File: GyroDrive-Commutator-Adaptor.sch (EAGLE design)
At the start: 30 parts, among them IC1 INA2141U, IC2 INA2141U, IC3 INA2141U

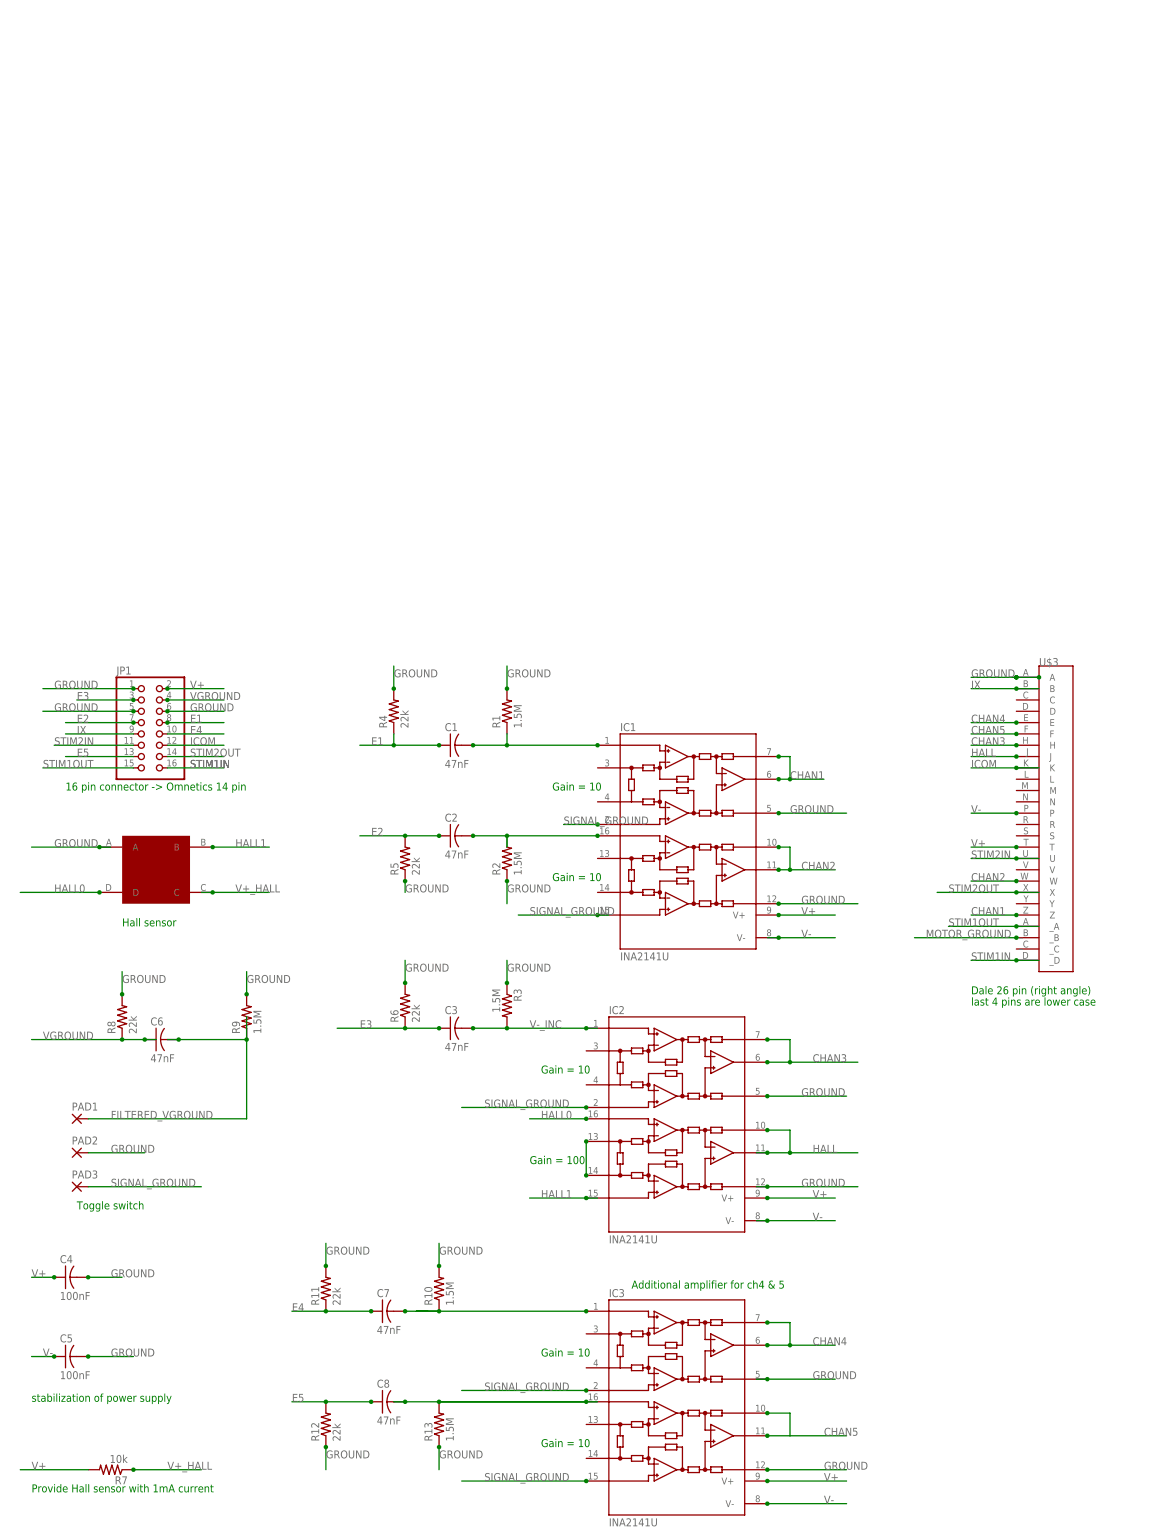
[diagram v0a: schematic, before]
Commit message: Removed VGROUND and changed JMP1 pinout
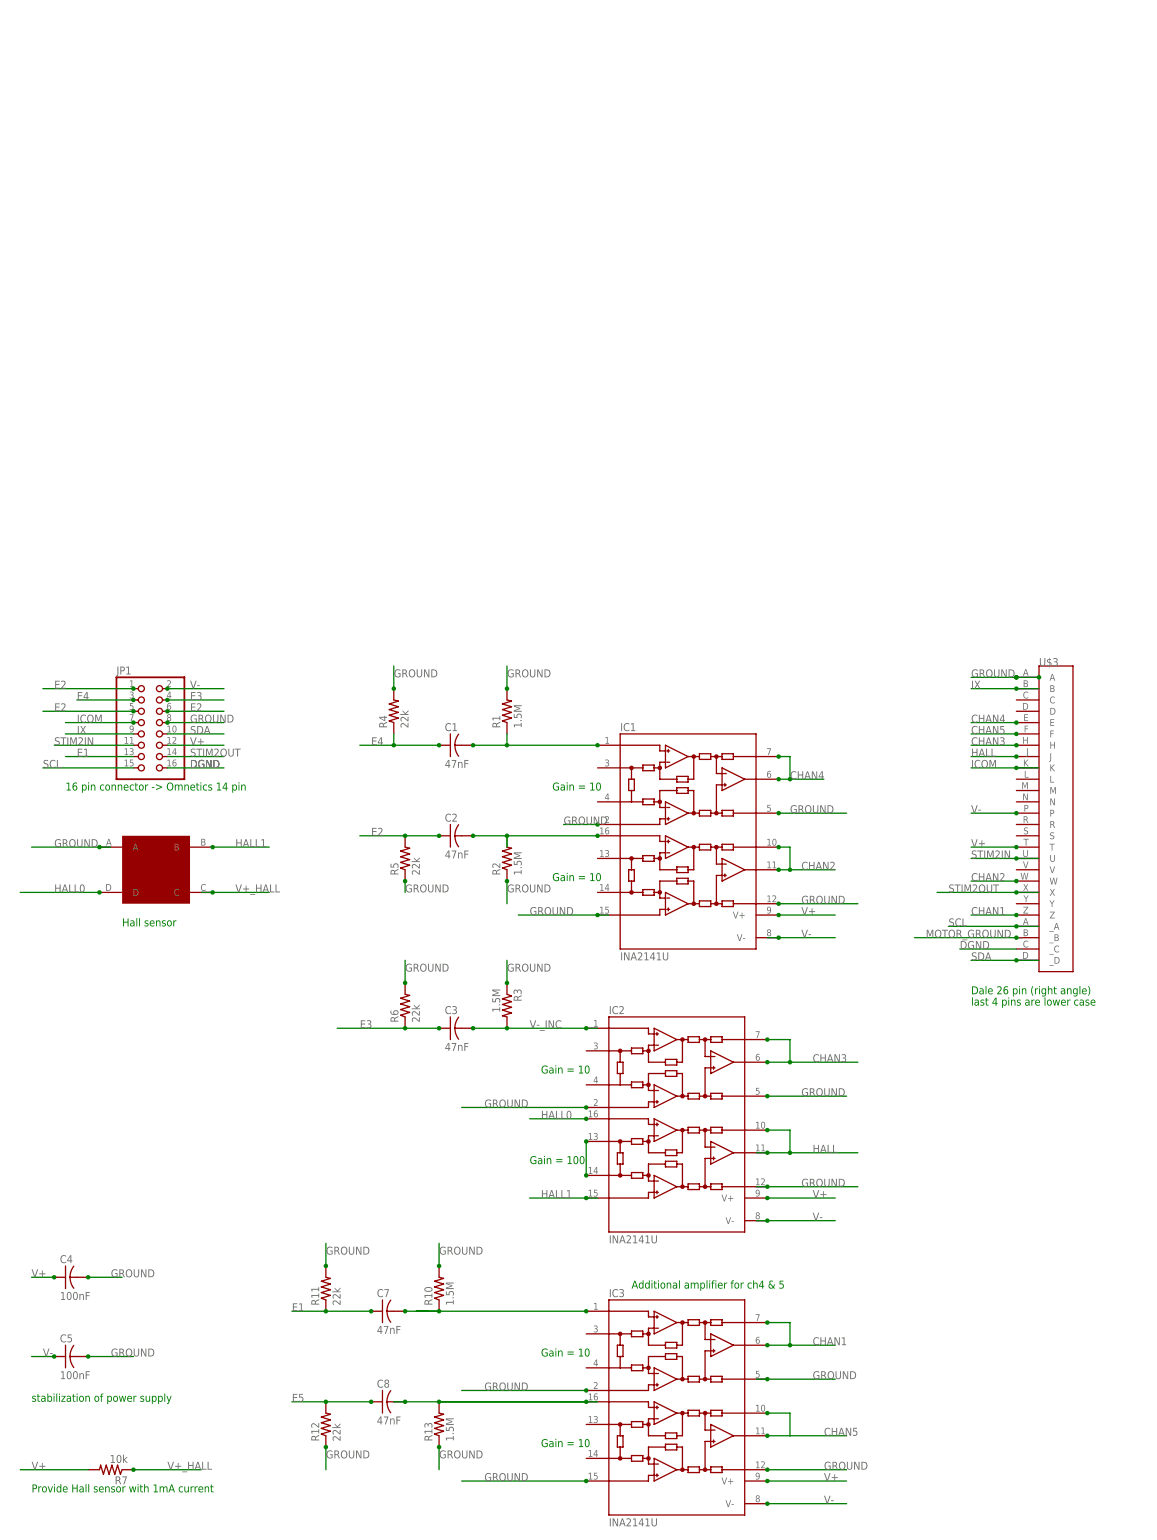
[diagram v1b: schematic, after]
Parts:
- removed C6: 47nF, elm:C0805ELM
- removed PAD1, PAD2, PAD3: (no value), wirepad:SMD2
- removed R8: 22k, elm:R0805ELM
- removed R9: 1.5M, elm:R0805ELM
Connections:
- net STIM1OUT renamed SCL
- removed net FILTERED_VGROUND: C6.2, PAD1.P, R9.1
- removed net SIGNAL_GROUND: IC1.INA+, IC1.INB+, IC2.INA+, IC3.INA+, IC3.INB+, PAD3.P
- removed net STIM1IN: JP1.16, U$3._D
- removed net VGROUND: C6.1, JP1.4, R8.1
- new net DGND: JP1.16, U$3._C
- new net SDA: JP1.10, U$3._D
- net CHAN1: now also IC3.SENSEA, IC3.VOA; no longer IC1.SENSEA, IC1.VOA
- net CHAN4: now also IC1.SENSEA, IC1.VOA; no longer IC3.SENSEA, IC3.VOA
- net E1: now also C7.1, JP1.13, R11.1; no longer C1.1, JP1.8, R4.1
- net E2: now also JP1.1, JP1.5, JP1.6; no longer JP1.7
- net E3: now also JP1.4; no longer JP1.3
- net E4: now also C1.1, JP1.3, R4.1; no longer C7.1, JP1.10, R11.1
- net E5: no longer JP1.13
- net GROUND: now also IC1.INA+, IC1.INB+, IC2.INA+, IC3.INA+, IC3.INB+, JP1.8; no longer JP1.1, JP1.5, JP1.6, PAD2.P, R8.2, R9.2
- net ICOM: now also JP1.7; no longer JP1.12
- net V+: now also JP1.12; no longer JP1.2
- net V-: now also JP1.2
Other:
- note removed: "Toggle switch"

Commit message: Made board into 4 layers. Put in resistors for voltage dividers
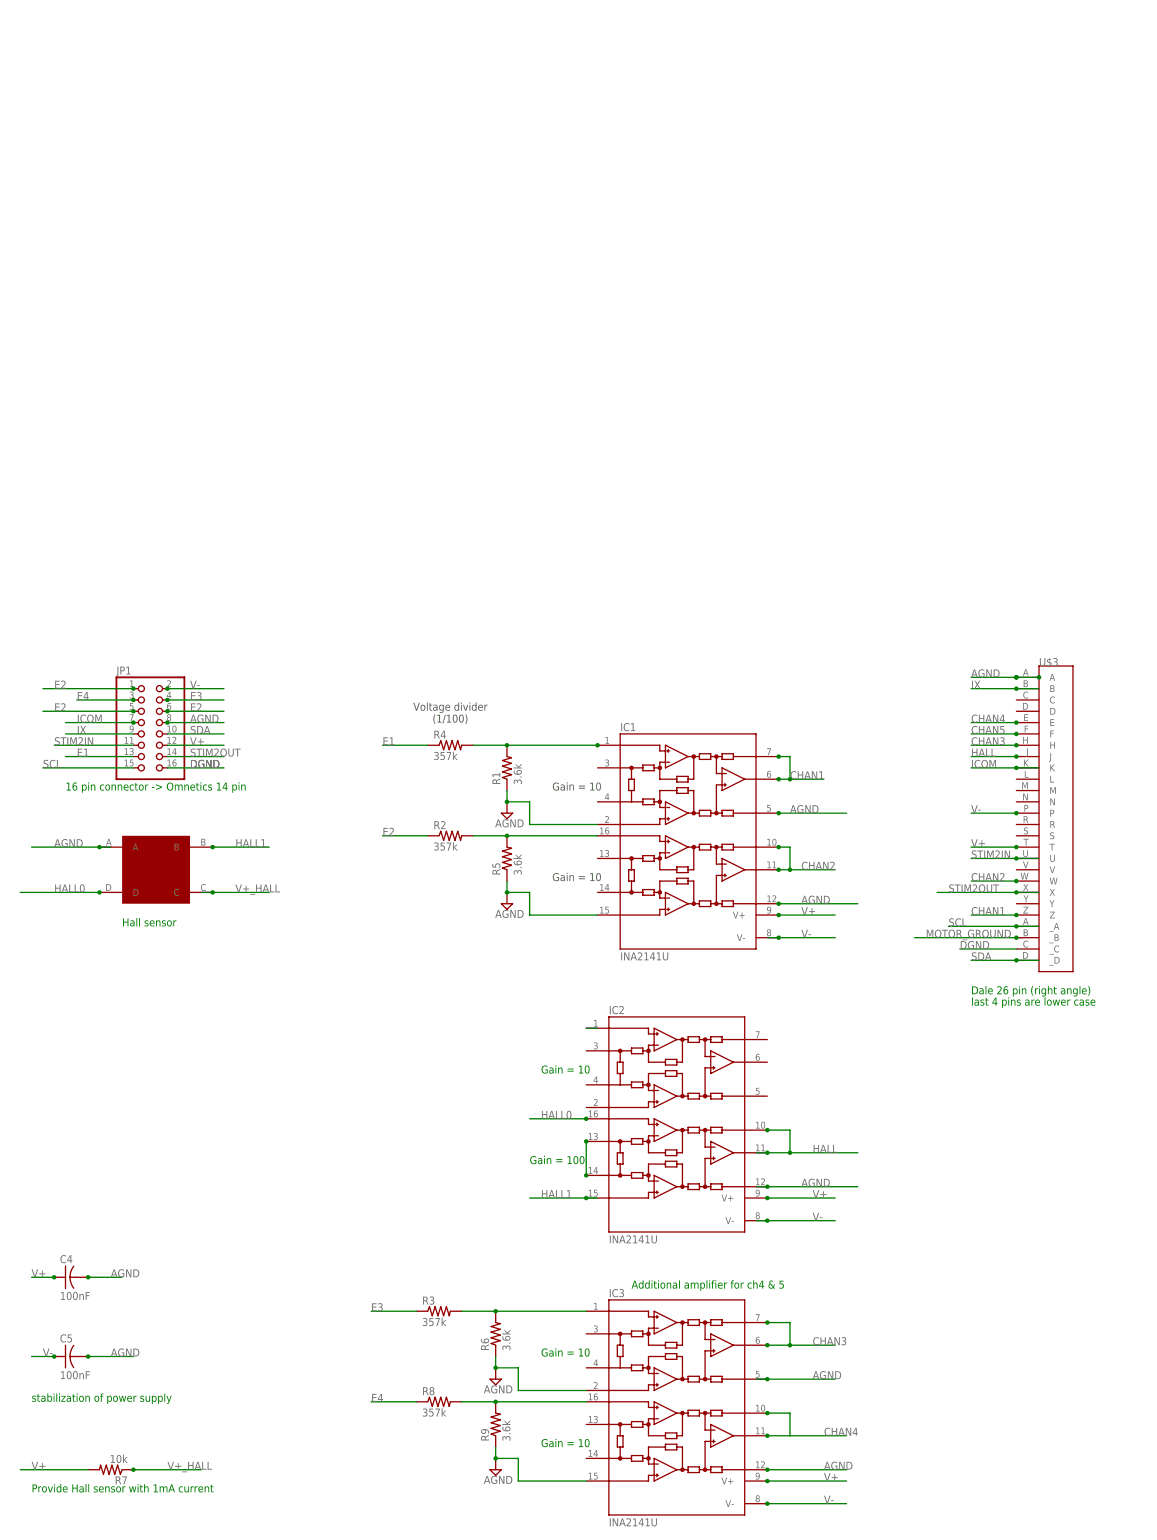
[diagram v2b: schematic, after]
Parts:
- removed C1, C2, C3, C7, C8: 47nF, elm:C0805ELM
- removed R10, R13: 1.5M, elm:R0805ELM
- removed R11, R12: 22k, elm:R0805ELM
- added R8: 357k, resistor:R-US_R0805
- added R9: 3.6k, resistor:R-US_R0805
- R1: value 1.5M -> 3.6k; device elm:R0805ELM -> resistor:R-US_R0805
- R2, R3: value 1.5M -> 357k; device elm:R0805ELM -> resistor:R-US_R0805
- R4: value 22k -> 357k; device elm:R0805ELM -> resistor:R-US_R0805
- R5, R6: value 22k -> 3.6k; device elm:R0805ELM -> resistor:R-US_R0805
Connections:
- removed net E5: C8.1, R12.2
- removed net GROUND: C4.2, C5.2, IC1.INA+, IC1.INB+, IC1.REFA, IC1.REFB, IC2.INA+, IC2.REFA, IC2.REFB, IC3.INA+, IC3.INB+, IC3.REFA, IC3.REFB, JP1.8, R1.2, R10.2, R11.2, R12.1, R13.1, R2.1, R3.1, R4.2, R5.1, R6.2, U$2.A, U$3.A
- removed net N$3: C2.2, IC1.INB-, R2.2
- removed net N$7: C8.2, IC3.INB-, R13.2
- removed net N$8: C7.2, IC3.INA-, R10.1
- new net AGND: C4.2, C5.2, IC1.INA+, IC1.INB+, IC1.REFA, IC1.REFB, IC2.REFB, IC3.INA+, IC3.INB+, IC3.REFA, IC3.REFB, JP1.8, R1.1, R5.1, R6.1, R9.1, U$2.A, U$3.A
- new net V-_INA1: IC1.INB-, R2.2, R5.2
- new net V-_INA2: IC3.INA-, R3.2, R6.2
- new net V-_INA3: IC3.INB-, R8.2, R9.2
- net CHAN1: now also IC1.SENSEA, IC1.VOA; no longer IC3.SENSEA, IC3.VOA
- net CHAN3: now also IC3.SENSEA, IC3.VOA; no longer IC2.SENSEA, IC2.VOA
- net CHAN4: now also IC3.SENSEB, IC3.VOB; no longer IC1.SENSEA, IC1.VOA
- net CHAN5: no longer IC3.SENSEB, IC3.VOB
- net E1: now also R4.1; no longer C7.1, R11.1
- net E2: now also R2.1; no longer C2.1, R5.2
- net E3: now also R3.1; no longer C3.1, R6.1
- net E4: now also R8.1; no longer C1.1, R4.1
- net V-_INA: now also R1.2, R4.2; no longer C1.2, R1.1
- net V-_INC: no longer C3.2, R3.2
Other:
- note added: "Voltage divider (1/100)"
- moved on the sheet: R1, R2, R3, R4, R5, R6

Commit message: Finished routing
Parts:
- removed U$3: MMD1P22G-26-M101, elm:MMD1P22G-26-M101
- added C1, C2, C3, C6: (no value), resistor:C-USC0402
- added U$1: NORCOMP-DB25-SMD-MALE, michael-stetner:NORCOMP-DB25-SMD-MALE
- added U4: PCA9517, PCA9517:PCA9517
- added U5: 5V, michael-stetner:TPS715-FIXED
- added U6: 2.5V, michael-stetner:TPS715-FIXED
- renumbered IC1 to U1, IC2 to U2, IC3 to U3
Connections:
- removed net CHAN5: U$3.F
- removed net GAIN_HALL: U2.JB, U2.JB@1
- removed net MOTOR_GROUND: U$3._B
- removed net SCL: JP1.15, U$3._A
- removed net SDA: JP1.10, U$3._D
- removed net STIM2IN: JP1.11, U$3.U
- removed net STIM2OUT: JP1.14, U$3.X
- removed net V-_INA: R1.2, R4.2, U1.INA-
- removed net V-_INA1: R2.2, R5.2, U1.INB-
- removed net V-_INA2: R3.2, R6.2, U3.INA-
- removed net V-_INA3: R8.2, R9.2, U3.INB-
- removed net V-_INC: U2.INA-
- new net +2.5V: C6.1, U4.VCCA, U6.OUT
- new net +5V: C1.1, U4.EN, U4.VCCB, U5.OUT
- new net IN1: R2.2, R5.1, U1.INB+
- new net IN2: R1.2, R4.2, U1.INA+
- new net IN3: R3.2, R6.1, U2.INB+
- new net IN4: R8.2, R9.1, U3.INA+
- new net MOTORGND: U$1.18
- new net N$1: U2.SENSEA, U2.VOA
- new net N$3: U3.JB, U3.JB@1
- new net SCL_BIRD: JP1.16, U4.SCLA
- new net SCL_RIG: U$1.22, U4.SCLB
- new net SDA_BIRD: JP1.15, U4.SDAA
- new net SDA_RIG: U$1.21, U4.SDAB
- new net STIMIN: JP1.5, U$1.23
- new net STIMOUT: JP1.3, U$1.24
- net AGND: now also JP1.10, JP1.11, R5.2, R6.2, R9.2, U$1.10, U1.INA-, U1.INB-, U2.INA+, U2.INA-, U2.INB-, U3.INA-; no longer JP1.8, R5.1, R6.1, R9.1, U$3.A, U1.INA+, U1.INB+, U3.INA+, U3.INB+
- net CHAN1: now also U$1.13, U1.SENSEB, U1.VOB; no longer U$3.Z, U1.SENSEA, U1.VOA
- net CHAN2: now also U$1.12, U1.SENSEA, U1.VOA; no longer U$3.W, U1.SENSEB, U1.VOB
- net CHAN3: now also U$1.11, U2.SENSEB, U2.VOB; no longer U$3.H, U3.SENSEA, U3.VOA
- net CHAN4: now also U$1.16, U3.SENSEA, U3.VOA; no longer U$3.E, U3.SENSEB, U3.VOB
- net DGND: now also C1.2, C2.2, C3.2, C6.2, JP1.13, JP1.14, U$1.15, U4.GND, U5.GND, U6.GND; no longer JP1.16, U$3._C
- net E1: now also JP1.1, R2.1; no longer JP1.13, R4.1
- net E2: now also JP1.2, R4.1; no longer JP1.1, JP1.5, JP1.6, R2.1
- net E4: now also JP1.12; no longer JP1.3
- net HALL: now also U$1.4, U3.SENSEB, U3.VOB; no longer U$3.J, U2.SENSEB, U2.VOB
- net HALL0: now also U3.INB-; no longer U2.INB-
- net HALL1: now also U3.INB+; no longer U2.INB+
- net ICOM: now also JP1.6, U$1.5; no longer JP1.7, U$3.K
- net IX: now also JP1.8, U$1.17; no longer JP1.9, U$3.B
- net V+: now also C2.1, C3.1, JP1.9, U$1.1, U5.IN, U6.IN; no longer JP1.12, U$3.T
- net V-: now also JP1.7, U$1.2; no longer JP1.2, U$3.P
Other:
- note added: "According to datasheet: "If channel is unused, connect inputs to ground, sense to Vo, and leave Ref open-circuit.""
- note added: "Unused"
- note removed: "Dale 26 pin (right angle)"
- note removed: "last 4 pins are lower case"
- moved on the sheet: R1, R2, R3, R4, R5, R6, R8, R9

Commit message: added parts list
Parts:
- removed U$2: HALL, elm:HALL_ON_SIDE
- added U7: INA2141U, burr-brown:INA2141U
- C4: value 100nF -> (none); device elm:C0805ELM -> resistor:C-USC0402
- C6: value (none) -> 100nF; device resistor:C-USC0402 -> elm:C0805ELM
- R1: value 3.6k -> 10k; device resistor:R-US_R0805 -> elm:R0805ELM
- R5: value 3.6k -> 357k
- R7: value 10k -> 3.6k; device elm:R0805ELM -> resistor:R-US_R0805
- R8: value 357k -> 3.6k
- U1: value INA2141U -> HALL; device burr-brown:INA2141U -> elm:HALL_ON_SIDE
- U2: value INA2141U -> PCA9517; device burr-brown:INA2141U -> PCA9517:PCA9517
- U3: value INA2141U -> 5V; device burr-brown:INA2141U -> michael-stetner:TPS715-FIXED
- U4: value PCA9517 -> 2.5V; device PCA9517:PCA9517 -> michael-stetner:TPS715-FIXED
- U5: value 5V -> INA2141U; device michael-stetner:TPS715-FIXED -> burr-brown:INA2141U
- U6: value 2.5V -> INA2141U; device michael-stetner:TPS715-FIXED -> burr-brown:INA2141U
- renumbered JP1 to X2, U$1 to X1
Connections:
- net +2.5V: now also C4.1, U2.VCCA, U4.OUT; no longer C6.1, U4.VCCA, U6.OUT
- net +5V: now also C3.1, U2.EN, U2.VCCB, U3.OUT; no longer C1.1, U4.EN, U4.VCCB, U5.OUT
- net AGND: now also C6.2, R6.1, R7.2, R8.2, U1.A, U5.INA-, U5.INB-, U5.REFA, U5.REFB, U6.INA+, U6.INA-, U6.INB-, U6.REFB, U7.INA-, U7.REFA, U7.REFB; no longer C4.2, R1.1, R5.2, R6.2, U$2.A, U1.INA-, U1.INB-, U1.REFA, U1.REFB, U2.INA+, U2.INA-, U2.INB-, U2.REFB, U3.INA-, U3.REFA, U3.REFB
- net CHAN1: now also U5.SENSEB, U5.VOB; no longer U1.SENSEB, U1.VOB
- net CHAN2: now also U5.SENSEA, U5.VOA; no longer U1.SENSEA, U1.VOA
- net CHAN3: now also U6.SENSEB, U6.VOB; no longer U2.SENSEB, U2.VOB
- net CHAN4: now also U7.SENSEA, U7.VOA; no longer U3.SENSEA, U3.VOA
- net DGND: now also C4.2, U2.GND, U3.GND; no longer C6.2, U5.GND, U6.GND
- net E1: now also R3.1; no longer R2.1
- net E2: now also R2.1; no longer R4.1
- net E3: now also R4.1; no longer R3.1
- net E4: now also R5.1; no longer R8.1
- net HALL: now also U7.SENSEB, U7.VOB; no longer U3.SENSEB, U3.VOB
- net HALL0: now also U1.D, U7.INB-; no longer U$2.D, U3.INB-
- net HALL1: now also U1.B, U7.INB+; no longer U$2.B, U3.INB+
- net IN1: now also R3.2, R7.1, U5.INB+; no longer R2.2, R5.1, U1.INB+
- net IN2: now also R2.2, R6.2, U5.INA+; no longer R1.2, R4.2, U1.INA+
- net IN3: now also R4.2, R8.1, U6.INB+; no longer R3.2, R6.1, U2.INB+
- net IN4: now also R5.2, U7.INA+; no longer R8.2, U3.INA+
- net N$1: now also U6.SENSEA, U6.VOA; no longer U2.SENSEA, U2.VOA
- net N$3: now also U7.JB, U7.JB@1; no longer U3.JB, U3.JB@1
- net SCL_BIRD: now also U2.SCLA; no longer U4.SCLA
- net SCL_RIG: now also U2.SCLB; no longer U4.SCLB
- net SDA_BIRD: now also U2.SDAA; no longer U4.SDAA
- net SDA_RIG: now also U2.SDAB; no longer U4.SDAB
- net V+: now also C1.1, C5.1, R1.2, U3.IN, U4.IN, U5.V+, U6.V+, U7.V+; no longer C3.1, C4.1, R7.2, U1.V+, U2.V+, U3.V+, U5.IN, U6.IN
- net V+_HALL: now also R1.1, U1.C; no longer R7.1, U$2.C
- net V-: now also C6.1, U5.V-, U6.V-, U7.V-; no longer C5.1, U1.V-, U2.V-, U3.V-
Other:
- moved on the sheet: C1, C2, C3, C5, R1, R2, R3, R4, R5, R6, R7, R8
